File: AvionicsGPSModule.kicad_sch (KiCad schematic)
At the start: 33 parts, among them P1 MC311D, Q1 AO3400A, U2 AP2112K-3.3, U3 L80-R, U4 RP2040, U6 W25Q128JVS, X1 ABM8-272-T3

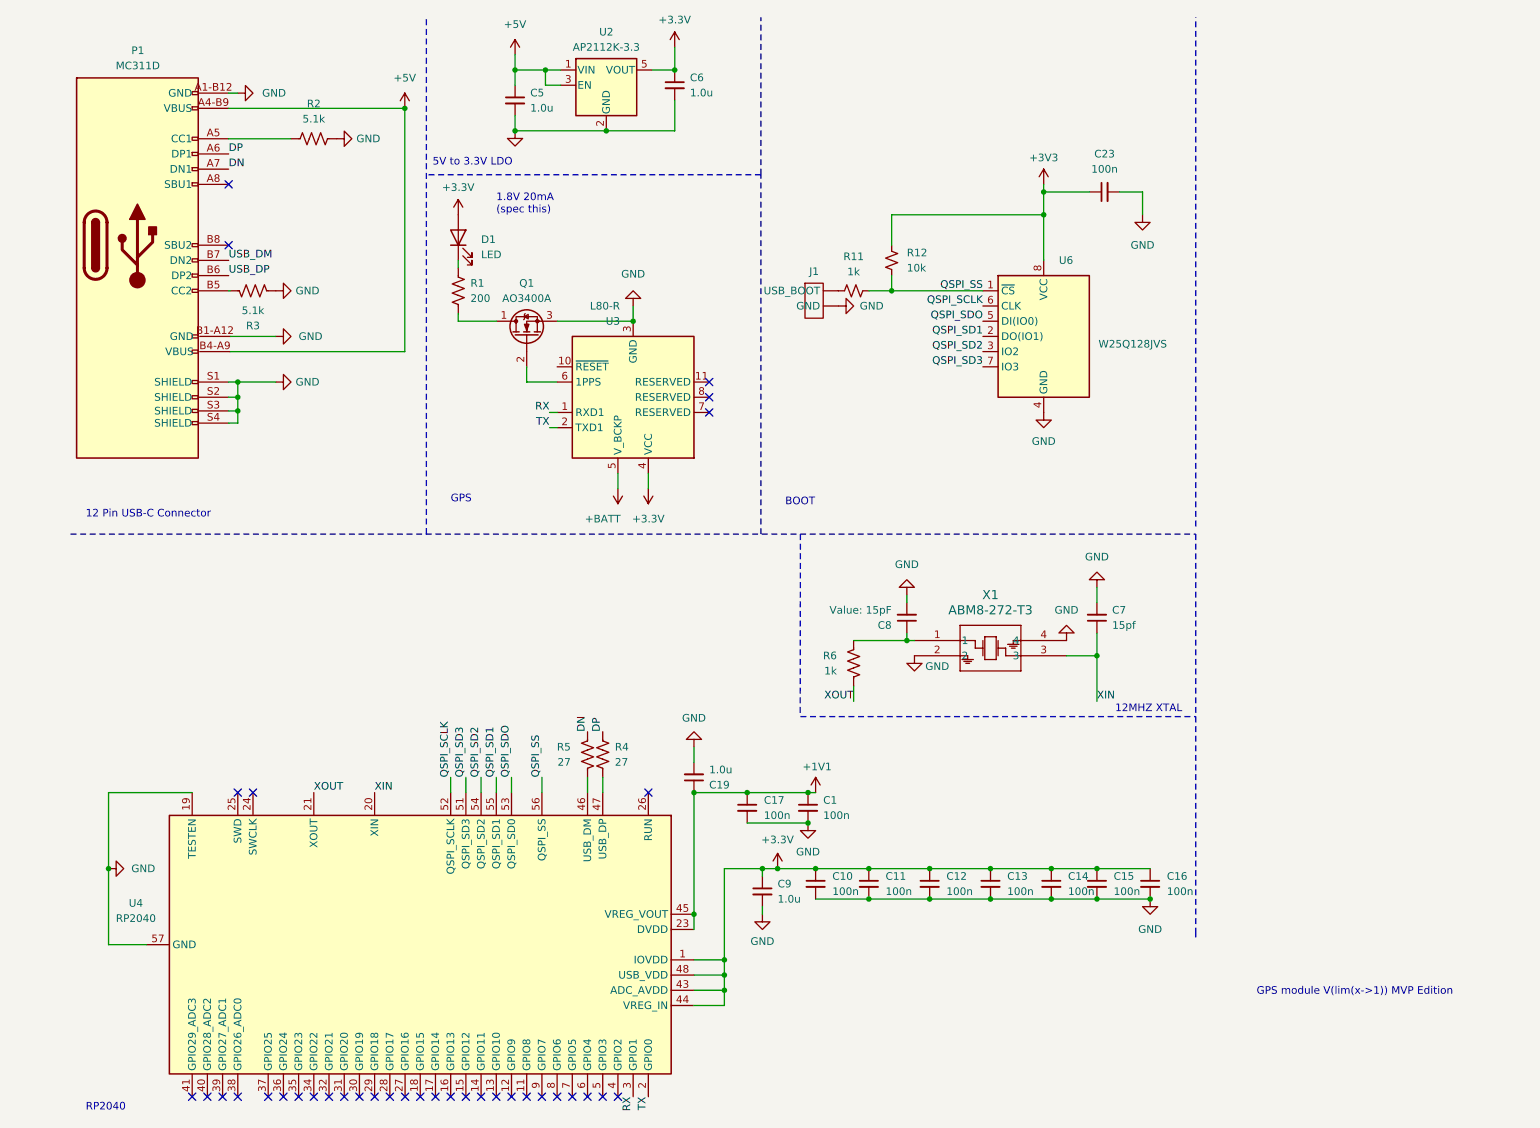
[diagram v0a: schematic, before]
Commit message: Fix: Moved RP2040 capacitors
Fix: Corrected Design Rules for clearance and width

Fix: Correctly Annotated capacitors
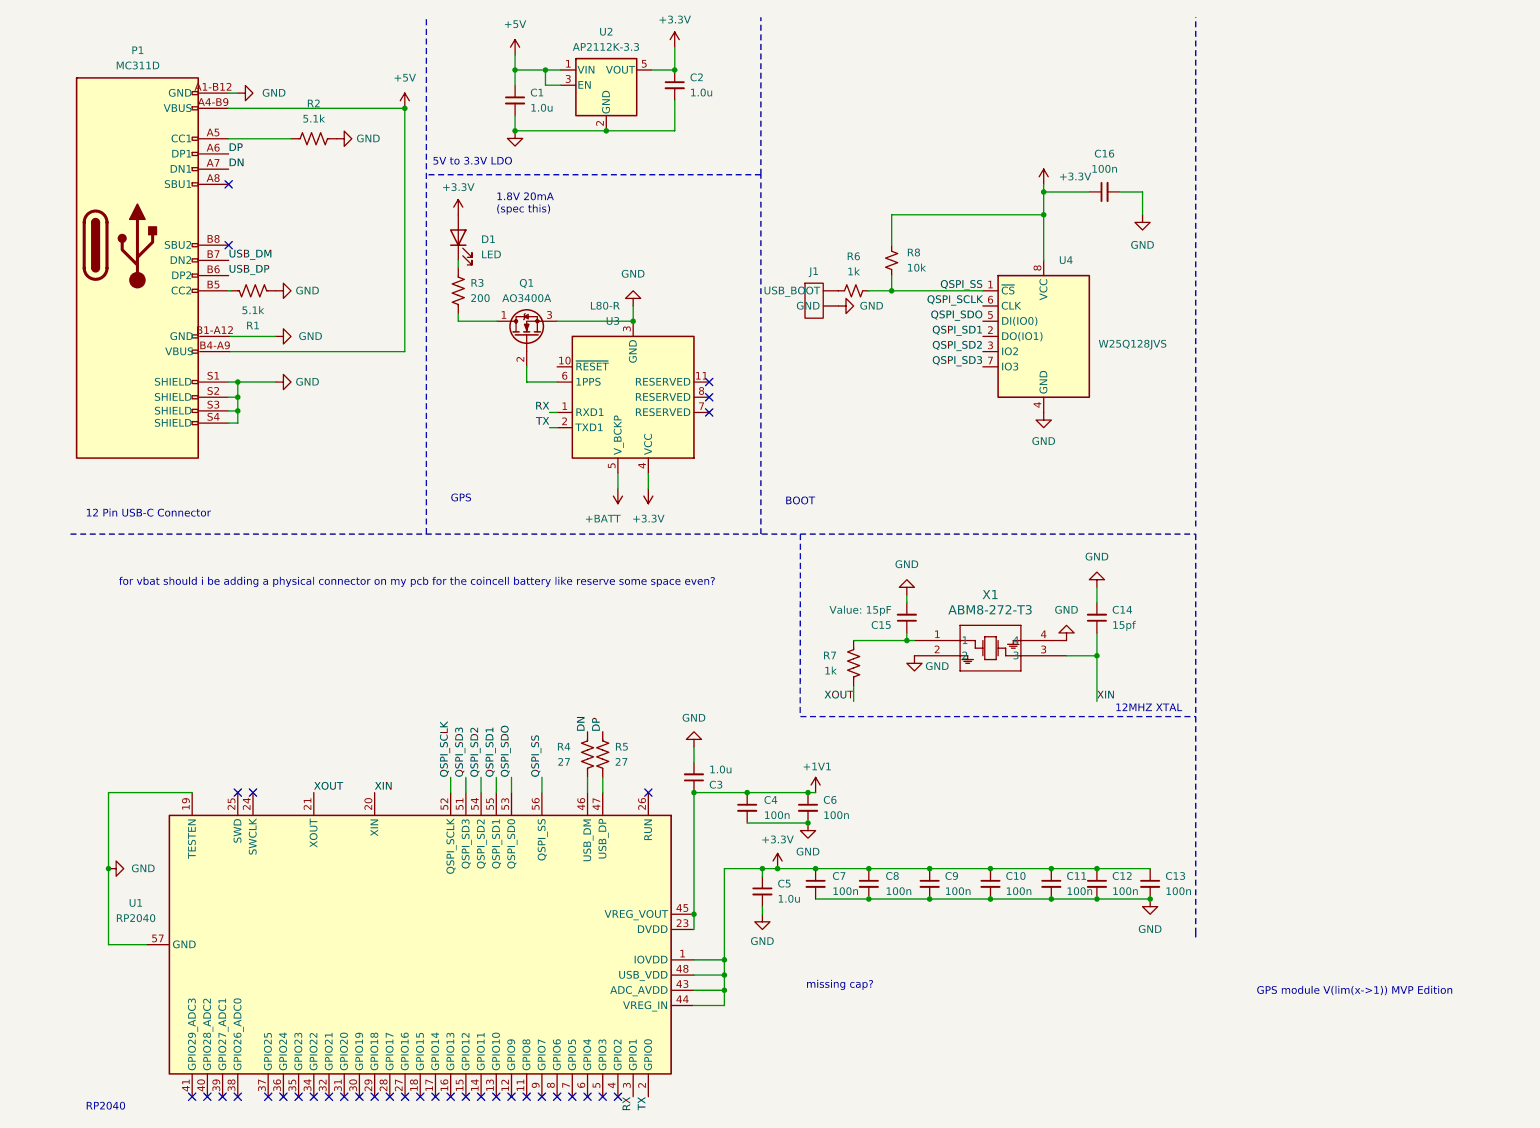
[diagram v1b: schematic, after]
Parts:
- renumbered C5 to C1, C13 to C10, C14 to C11, C15 to C12, C16 to C13, C7 to C14, C8 to C15, C23 to C16, C6 to C2, C19 to C3, C17 to C4, C9 to C5, C1 to C6, C10 to C7, C11 to C8, C12 to C9, R3 to R1, R1 to R3, R5 to R4, R4 to R5, R11 to R6, R6 to R7, R12 to R8, U4 to U1, U6 to U4
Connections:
- net +3V3 is gone; now on net +3.3V: C16.1, R8.1, U4.8 (VCC)
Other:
- note added: "for vbat should i be adding a physical connector on my pcb for the coincell battery like reserve some space even?"
- note added: "missing cap?"

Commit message: finalized wiring
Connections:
- net +3.3V: now also D1.1 (K); no longer D1.2 (A)
- net at R3.1: now also D1.2 (A); no longer D1.1 (K)
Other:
- moved on the sheet: C16, Q1, R3, R8, U3
